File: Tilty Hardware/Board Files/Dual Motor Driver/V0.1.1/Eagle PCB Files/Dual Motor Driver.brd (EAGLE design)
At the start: 38.4 x 50.8 mm, 42 parts, among them J1 AVR_SPI_PRG_62X3_LOCK, Q1 16MHz, U1 ATMEGA328P, U2 L298_BRIDGE_DRIVER, U3 LM2931

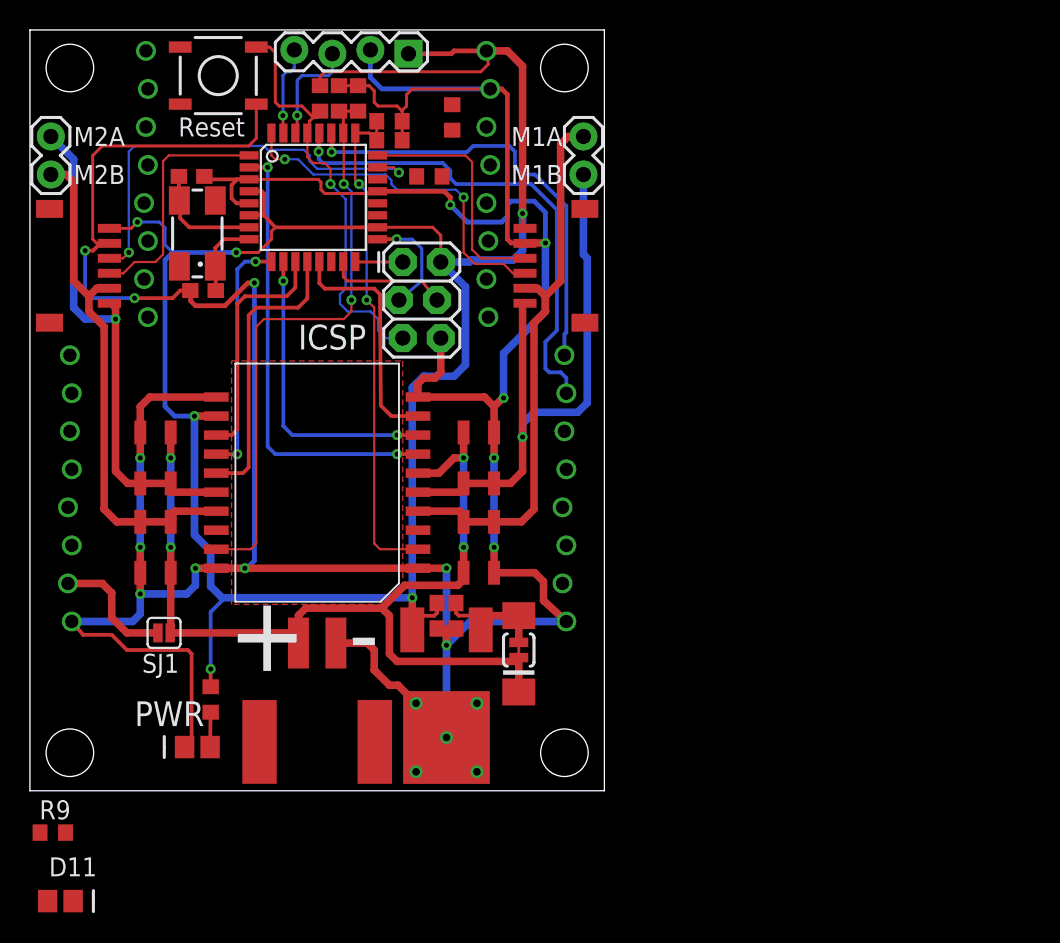
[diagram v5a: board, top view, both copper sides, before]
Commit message: Changes to Dual Motor Driver add-on
Moved some res and caps around.
Added a status LED.
Added silkscreen to rectifier diodes to show orientations.
Added I2C pullup resistors.
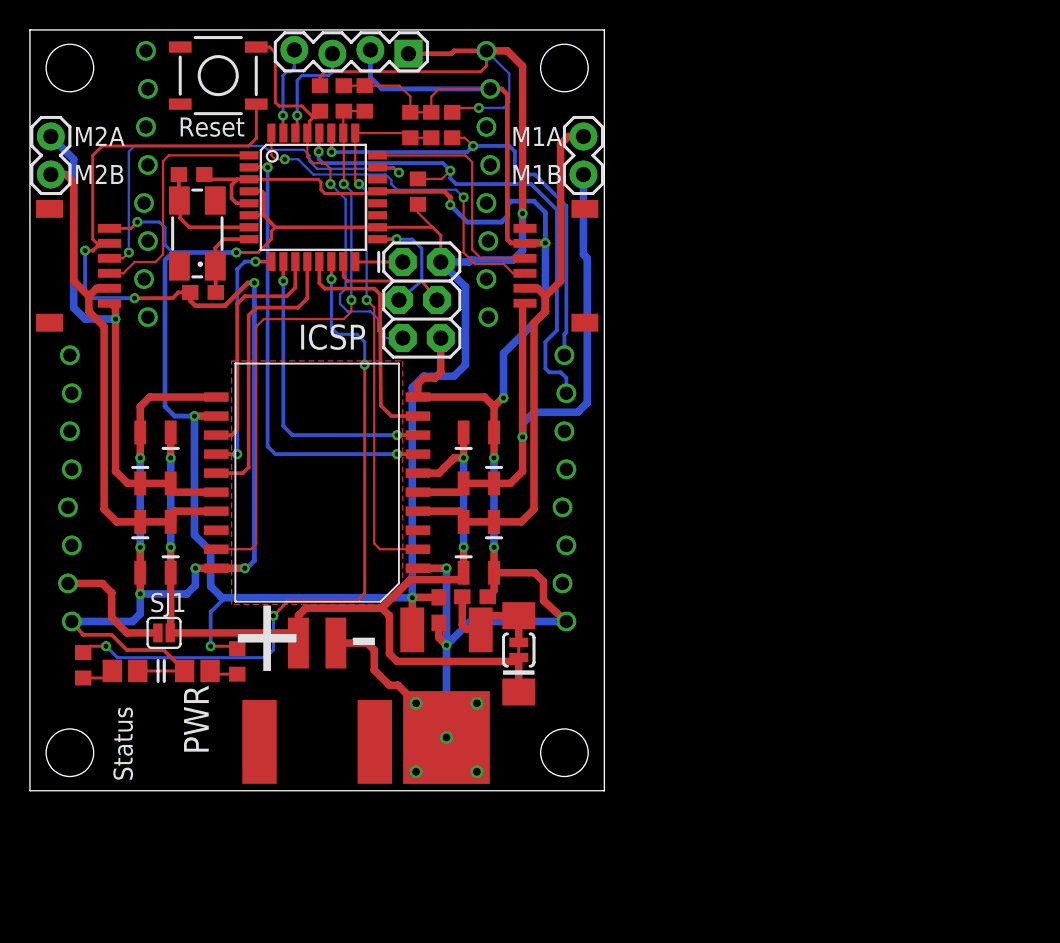
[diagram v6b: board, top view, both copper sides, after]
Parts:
- moved D11 16.0 mm to (6.35, 8.00)
- moved R9 11.4 mm to (3.56, 8.38), turned to 270 degrees
- moved D10 5.08 mm to (11.2, 8.00)
- moved R6 3.10 mm to (13.8, 8.64)
- moved R3 2.97 mm to (26.8, 44.5), turned to 270 degrees
- moved C7 1.80 mm to (29.7, 13.0), turned to 0 degrees
- moved R2 1.42 mm to (25.4, 44.5), turned to 270 degrees
- moved R8 1.27 mm to (25.9, 40.0), turned to 270 degrees
- moved R7 0.51 mm to (28.2, 44.5)
- moved R4 0.44 mm to (22.4, 46.2)
- moved C6 0.40 mm to (27.3, 12.1)
- moved R5 0.32 mm to (21.0, 46.2)
- moved C2 0.13 mm to (11.6, 33.3)
- moved C8 0.13 mm to (10.8, 41.1)
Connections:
- new net N$2: D11.1, R9.2
- new net N$4: R9.1, U1.14
- net GND: now also D11.2
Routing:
- net N$4: track 0.00 -> 46.2 mm, vias 0 -> 4
- net GND: track 274.5 -> 259.0 mm
- net +5V: track 148.8 -> 157.9 mm, vias 6 -> 7
- net SCL: track 32.9 -> 35.3 mm, vias 1 -> 2
- net SENSE_1: track 33.9 -> 36.2 mm
- net N$2: track 0.00 -> 2.14 mm
- net SDA: track 29.4 -> 31.0 mm, vias 1 -> 2
- net N$3: track 7.67 -> 8.52 mm
- net +24V: track 63.7 -> 64.4 mm
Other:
- board text added: "Status"
